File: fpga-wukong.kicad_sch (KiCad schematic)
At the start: 2 parts, among them J4 Conn_02x32_Odd_Even, J5 Conn_02x32_Odd_Even

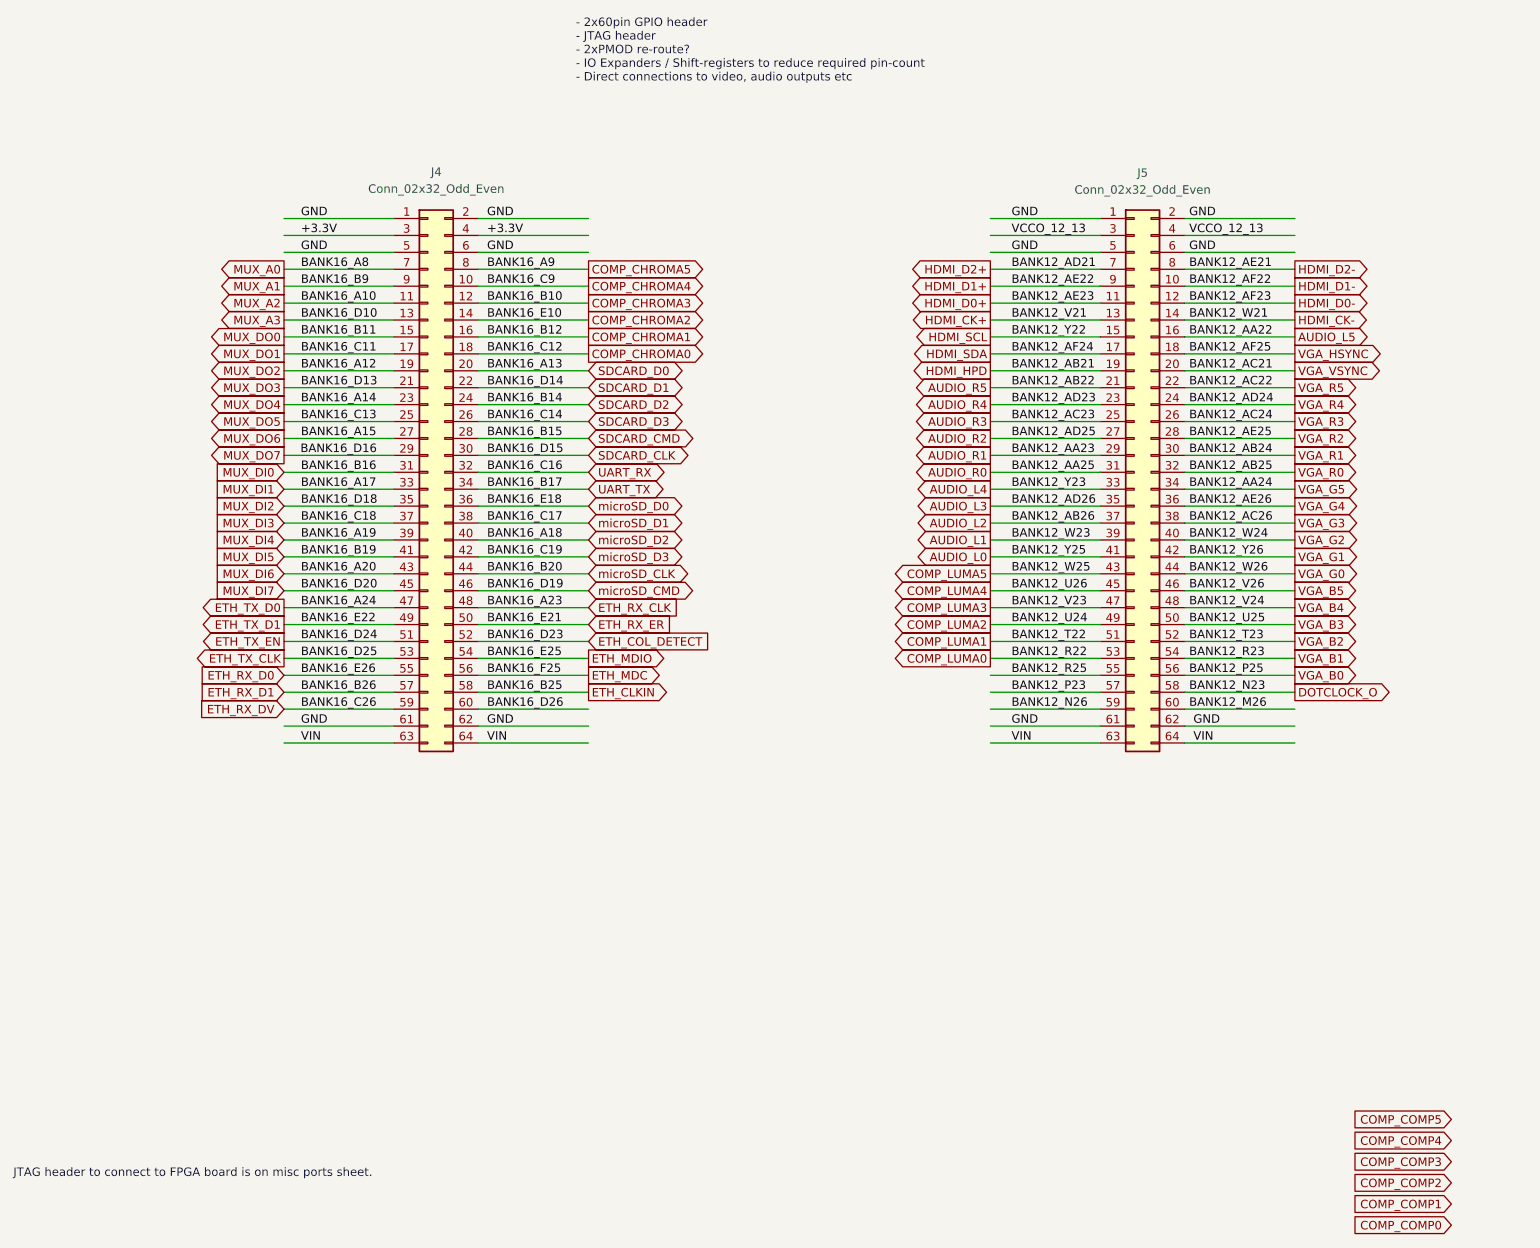
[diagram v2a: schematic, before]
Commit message: beautify the schematics, especially the title-page
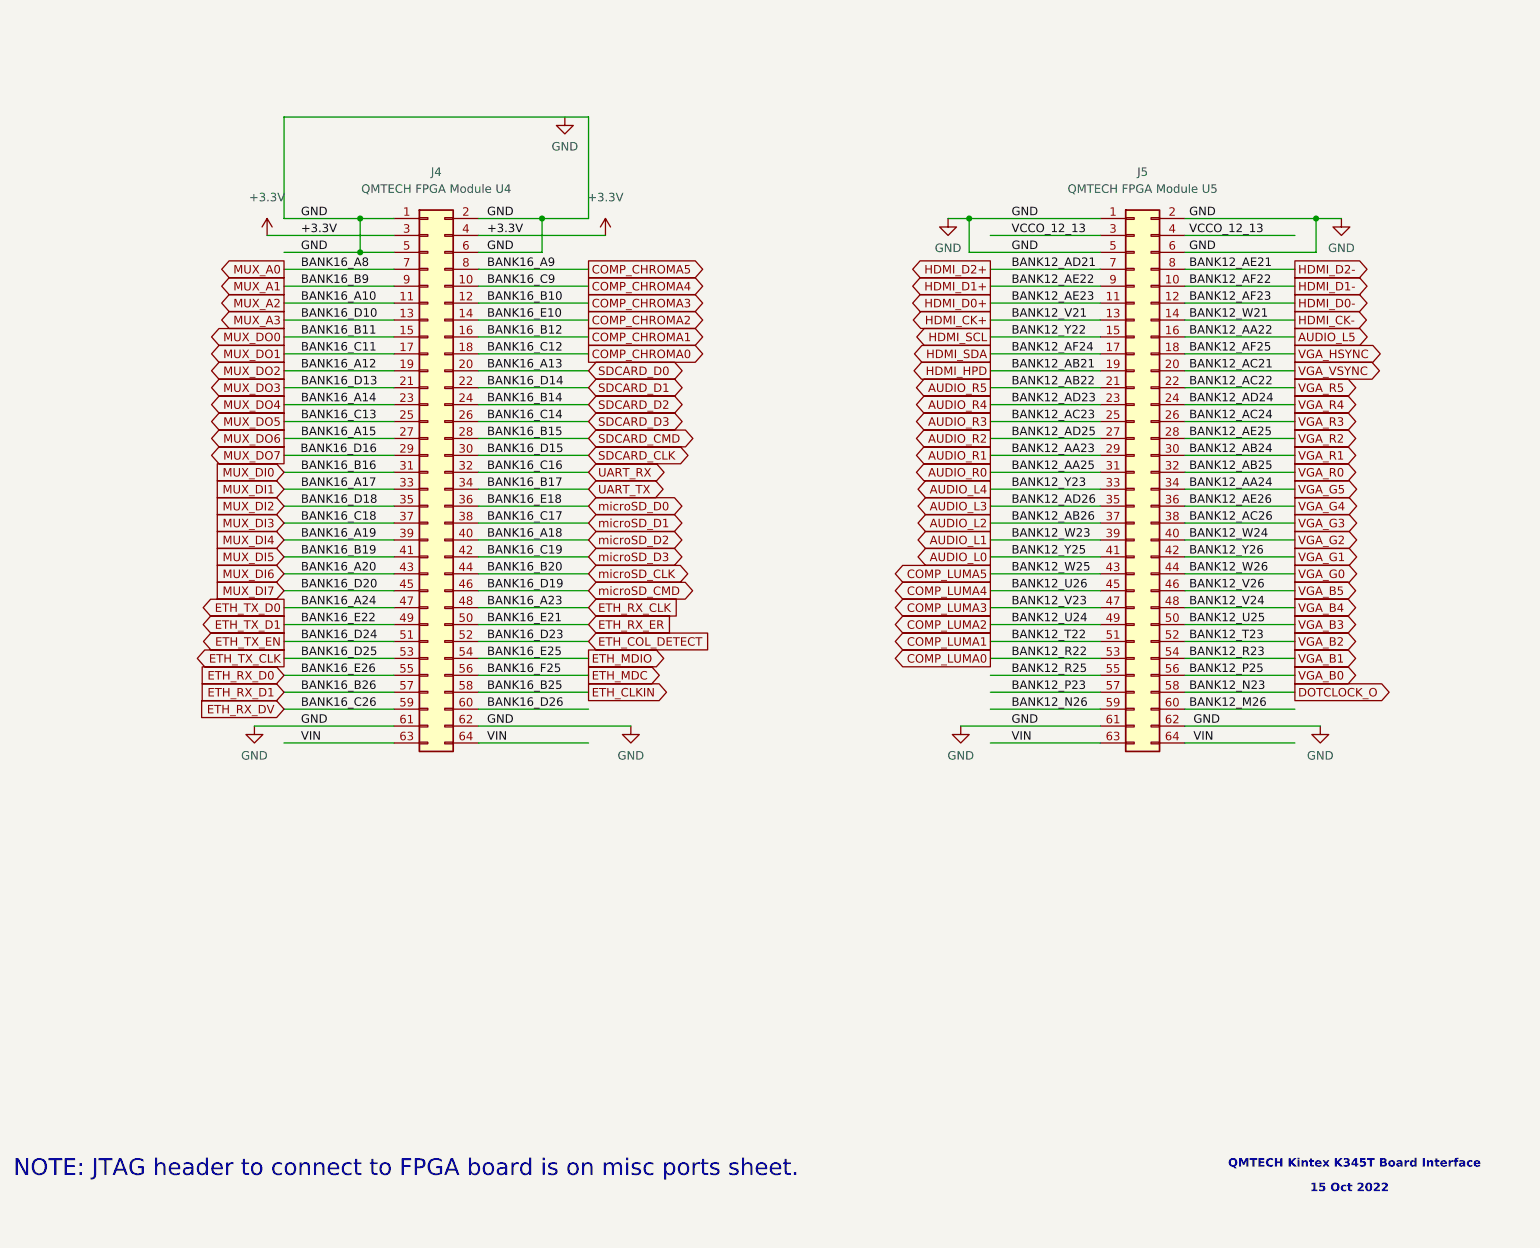
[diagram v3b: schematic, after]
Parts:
- J4: value Conn_02x32_Odd_Even -> QMTECH FPGA Module U4
- J5: value Conn_02x32_Odd_Even -> QMTECH FPGA Module U5
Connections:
- net +3.3V renamed +3V3
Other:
- note added: "15 Oct 2022"
- note added: "NOTE: JTAG header to connect to FPGA board is on misc ports sheet."
- note added: "QMTECH Kintex K345T Board Interface"
- note removed: "- 2x60pin GPIO header - JTAG header - 2xPMOD re-route? - IO Expanders / Shift-registers to reduce required pin-count - Direct connections to video, audio outputs etc"
- note removed: "JTAG header to connect to FPGA board is on misc ports sheet."

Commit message: add all missing footprints
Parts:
- J4, J5: footprint (none) -> Connector_PinHeader_2.54mm:PinHeader_2x32_P2.54mm_Vertical
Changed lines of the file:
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@@
   (symbol (lib_id "power:+3.3V") (at 57.785 50.165 0) (unit 1)
     (in_bom yes) (on_board yes) (fields_autoplaced)
-    (property "Reference" "#PWR?" (id 0) (at 57.785 53.975 0)
+    (property "Reference" "#PWR0189" (id 0) (at 57.785 53.975 0)
       (effects (font (size 1.27 1.27)) hide)
     )
@@
     (property "Reference" "J4" (id 0) (at 83.185 40.64 0))
     (property "Value" "QMTECH FPGA Module U4" (id 1) (at 83.185 43.18 0))
-    (property "Footprint" "" (id 2) (at 81.915 85.725 0)
+    (property "Footprint" "Connector_PinHeader_2.54mm:PinHeader_2x32_P2.54mm_Vertical" (id 2) (at 81.915 85.725 0)
       (effects (font (size 1.27 1.27)) hide)
     )
@@
   (symbol (lib_id "power:GND") (at 102.489 32.385 0) (unit 1)
     (in_bom yes) (on_board yes) (fields_autoplaced)
-    (property "Reference" "#PWR?" (id 0) (at 102.489 38.735 0)
+    (property "Reference" "#PWR0190" (id 0) (at 102.489 38.735 0)
       (effects (font (size 1.27 1.27)) hide)
     )
@@
     (property "Reference" "J5" (id 0) (at 189.23 40.64 0))
     (property "Value" "QMTECH FPGA Module U5" (id 1) (at 189.23 43.18 0))
-    (property "Footprint" "" (id 2) (at 187.96 85.725 0)
+    (property "Footprint" "Connector_PinHeader_2.54mm:PinHeader_2x32_P2.54mm_Vertical" (id 2) (at 187.96 85.725 0)
       (effects (font (size 1.27 1.27)) hide)
     )
@@
   (symbol (lib_id "power:GND") (at 215.9 123.825 0) (unit 1)
     (in_bom yes) (on_board yes) (fields_autoplaced)
-    (property "Reference" "#PWR?" (id 0) (at 215.9 130.175 0)
+    (property "Reference" "#PWR0194" (id 0) (at 215.9 130.175 0)
       (effects (font (size 1.27 1.27)) hide)
     )
@@
   (symbol (lib_id "power:GND") (at 55.88 123.825 0) (unit 1)
     (in_bom yes) (on_board yes) (fields_autoplaced)
-    (property "Reference" "#PWR?" (id 0) (at 55.88 130.175 0)
+    (property "Reference" "#PWR0187" (id 0) (at 55.88 130.175 0)
       (effects (font (size 1.27 1.27)) hide)
     )
@@
   (symbol (lib_id "power:+3.3V") (at 108.585 50.165 0) (unit 1)
     (in_bom yes) (on_board yes) (fields_autoplaced)
-    (property "Reference" "#PWR?" (id 0) (at 108.585 53.975 0)
+    (property "Reference" "#PWR0191" (id 0) (at 108.585 53.975 0)
       (effects (font (size 1.27 1.27)) hide)
     )
@@
   (symbol (lib_id "power:GND") (at 112.395 123.825 0) (unit 1)
     (in_bom yes) (on_board yes) (fields_autoplaced)
-    (property "Reference" "#PWR?" (id 0) (at 112.395 130.175 0)
+    (property "Reference" "#PWR0188" (id 0) (at 112.395 130.175 0)
       (effects (font (size 1.27 1.27)) hide)
     )
@@
   (symbol (lib_id "power:GND") (at 219.075 47.625 0) (unit 1)
     (in_bom yes) (on_board yes) (fields_autoplaced)
-    (property "Reference" "#PWR?" (id 0) (at 219.075 53.975 0)
+    (property "Reference" "#PWR0192" (id 0) (at 219.075 53.975 0)
       (effects (font (size 1.27 1.27)) hide)
     )
@@
   (symbol (lib_id "power:GND") (at 160.02 47.625 0) (unit 1)
     (in_bom yes) (on_board yes) (fields_autoplaced)
-    (property "Reference" "#PWR?" (id 0) (at 160.02 53.975 0)
+    (property "Reference" "#PWR0195" (id 0) (at 160.02 53.975 0)
       (effects (font (size 1.27 1.27)) hide)
     )
@@
   (symbol (lib_id "power:GND") (at 161.925 123.825 0) (unit 1)
     (in_bom yes) (on_board yes) (fields_autoplaced)
-    (property "Reference" "#PWR?" (id 0) (at 161.925 130.175 0)
-      (effects (font (size 1.27 1.27)) hide)
-    )
+    (property "Reference" "#PWR0193" (id 0) (at 161.925 130.175 0)
+      (effects (font (size 1.27 1.27)) hide)
+    )

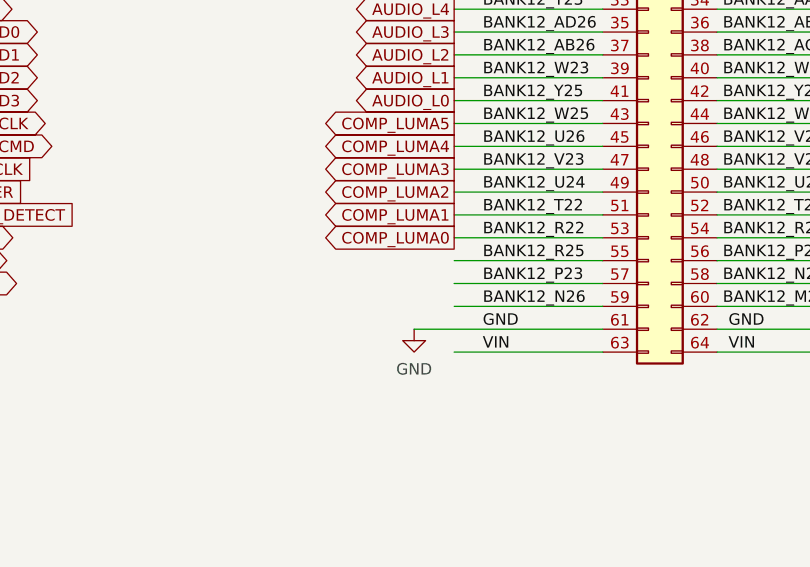
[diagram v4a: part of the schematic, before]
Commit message: add missing MEGA65 keyboard connector and keyboard JTAG header #10 #12
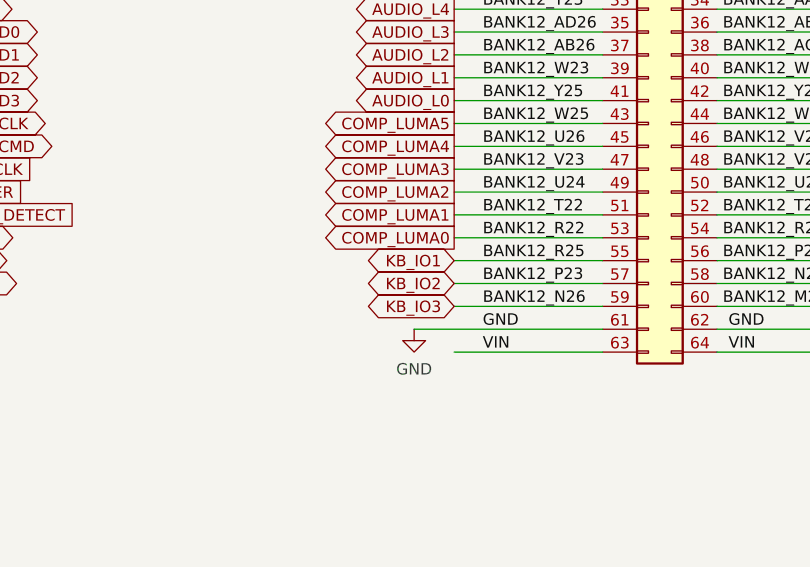
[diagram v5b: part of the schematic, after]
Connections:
- net BANK12_N26 renamed KB_IO3
- net BANK12_P23 renamed KB_IO2
- net BANK12_R25 renamed KB_IO1
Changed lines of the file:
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@@
+    )
+  )
+  (global_label "KB_IO2" (shape bidirectional) (at 166.37 118.745 180) (fields_autoplaced)
+    (effects (font (size 1.27 1.27)) (justify right))
+    (property "Intersheet References" "${INTERSHEET_REFS}" (id 0) (at 157.3045 118.6656 0)
+      (effects (font (size 1.27 1.27)) (justify right) hide)
     )
   )
@@
     )
   )
+  (global_label "KB_IO3" (shape bidirectional) (at 166.37 121.285 180) (fields_autoplaced)
+    (effects (font (size 1.27 1.27)) (justify right))
+    (property "Intersheet References" "${INTERSHEET_REFS}" (id 0) (at 157.3045 121.2056 0)
+      (effects (font (size 1.27 1.27)) (justify right) hide)
+    )
+  )
   (global_label "HDMI_D1+" (shape output) (at 166.37 57.785 180) (fields_autoplaced)
     (effects (font (size 1.27 1.27)) (justify right))
@@
     )
   )
+  (global_label "KB_IO1" (shape bidirectional) (at 166.37 116.205 180) (fields_autoplaced)
+    (effects (font (size 1.27 1.27)) (justify right))
+    (property "Intersheet References" "${INTERSHEET_REFS}" (id 0) (at 157.3045 116.1256 0)
+      (effects (font (size 1.27 1.27)) (justify right) hide)
+    )
+  )
